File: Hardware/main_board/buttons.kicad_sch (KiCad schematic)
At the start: 0 parts

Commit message: sch: done buttons
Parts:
- added C77, C78: 10uF, symbol Device:C
- added C79: 100nF, symbol Device:C
- added D1, D2, D3, D4, D5, D6: TVS, symbol Device:D_TVS
- added D7, D8, D9: 1N4148, symbol Device:D
- added R20, R21, R22, R23, R24, R25, R35: 10K, symbol Device:R_US
- added R26, R27, R28, R29, R30, R31, R34: 330R, symbol Device:R_US
- added R32, R33: 100K, symbol Device:R_US
- added SW1: OK, symbol Switch:SW_Push
- added SW2: BACK, symbol Switch:SW_Push
- added SW3: RIGHT, symbol Switch:SW_Push
- added SW4: LEFT, symbol Switch:SW_Push
- added SW5: UP, symbol Switch:SW_Push
- added SW6: DOWN, symbol Switch:SW_Push
- added U12: NC7SZ32M5X, symbol 74xGxx:74AHC1G32
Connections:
- new net: C78.2, D8.1 (K), R33.1, U12.2
- new net: D3.2 (A2), R22.1, R28.2, SW3.1
- new net: D5.2 (A2), R24.1, R30.2, SW5.1
- new net: D1.2 (A2), R20.2, R26.2, SW1.1
- new net: C77.2, D7.1 (K), R32.1, U12.1
- new net: D6.2 (A2), R25.1, R31.2, SW6.1
- new net: D9.1 (K), U12.4
- new net: D9.2 (A), R34.2
- new net +3.3V: C79.1, R21.2, R22.2, R23.2, R24.2, R25.2, R35.2, SW1.2, U12.5 (VCC)
- new net BACK: D2.2 (A2), D7.2 (A), R21.1, R27.2, R32.2, SW2.1
- new net BUTTON_BACK: R27.1
- new net BUTTON_DOWN: R31.1
- new net BUTTON_LEFT: R28.1
- new net BUTTON_OK: R26.1
- new net BUTTON_RIGHT: R29.1
- new net BUTTON_UP: R30.1
- new net GND: C77.1, C78.1, C79.2, D1.1 (A1), D2.1 (A1), D3.1 (A1), D4.1 (A1), D5.1 (A1), D6.1 (A1), R20.1, SW2.2, SW3.2, SW4.2, SW5.2, SW6.2, U12.3 (GND)
- new net LEFT: D4.2 (A2), D8.2 (A), R23.1, R29.2, R33.2, SW4.1
- new net RESET: R34.1, R35.1
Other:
- note added: "Buttons"
- note added: "RESET"

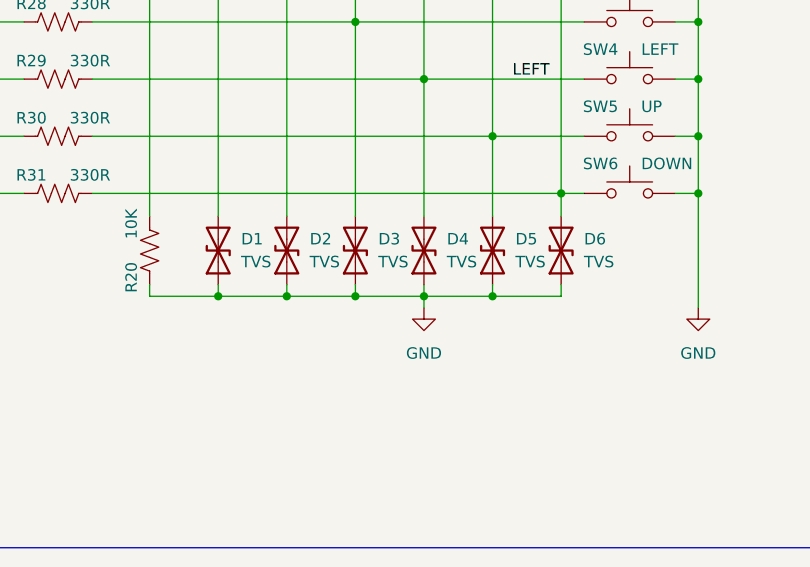
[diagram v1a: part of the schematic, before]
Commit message: sch: unify label style
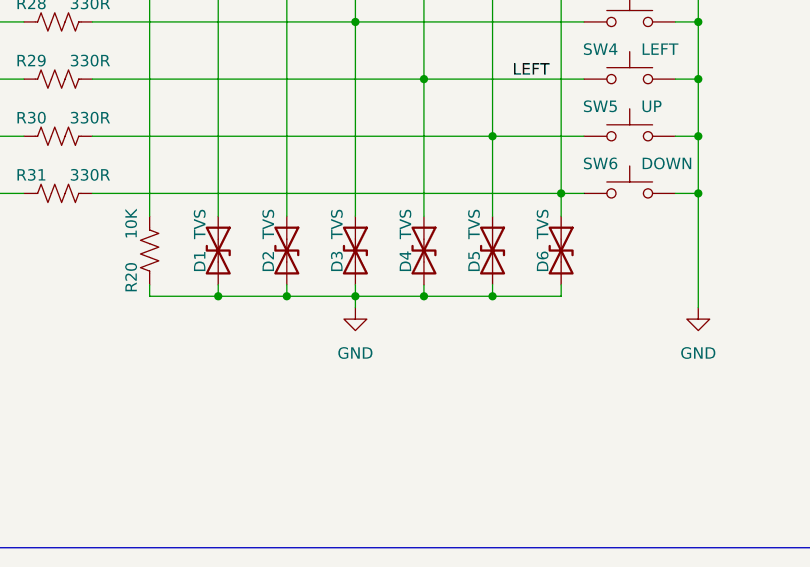
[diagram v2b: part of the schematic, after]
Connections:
- net BACK: now also D2.1 (A1); no longer D2.2 (A2)
- net GND: now also D1.2 (A2), D2.2 (A2), D3.2 (A2), D4.2 (A2), D5.2 (A2), D6.2 (A2); no longer D1.1 (A1), D2.1 (A1), D3.1 (A1), D4.1 (A1), D5.1 (A1), D6.1 (A1)
- net LEFT: now also D4.1 (A1); no longer D4.2 (A2)
- net at R22.1, R28.2, SW3.1: now also D3.1 (A1); no longer D3.2 (A2)
- net at R24.1, R30.2, SW5.1: now also D5.1 (A1); no longer D5.2 (A2)
- net at R20.2, R26.2, SW1.1: now also D1.1 (A1); no longer D1.2 (A2)
- net at R25.1, R31.2, SW6.1: now also D6.1 (A1); no longer D6.2 (A2)

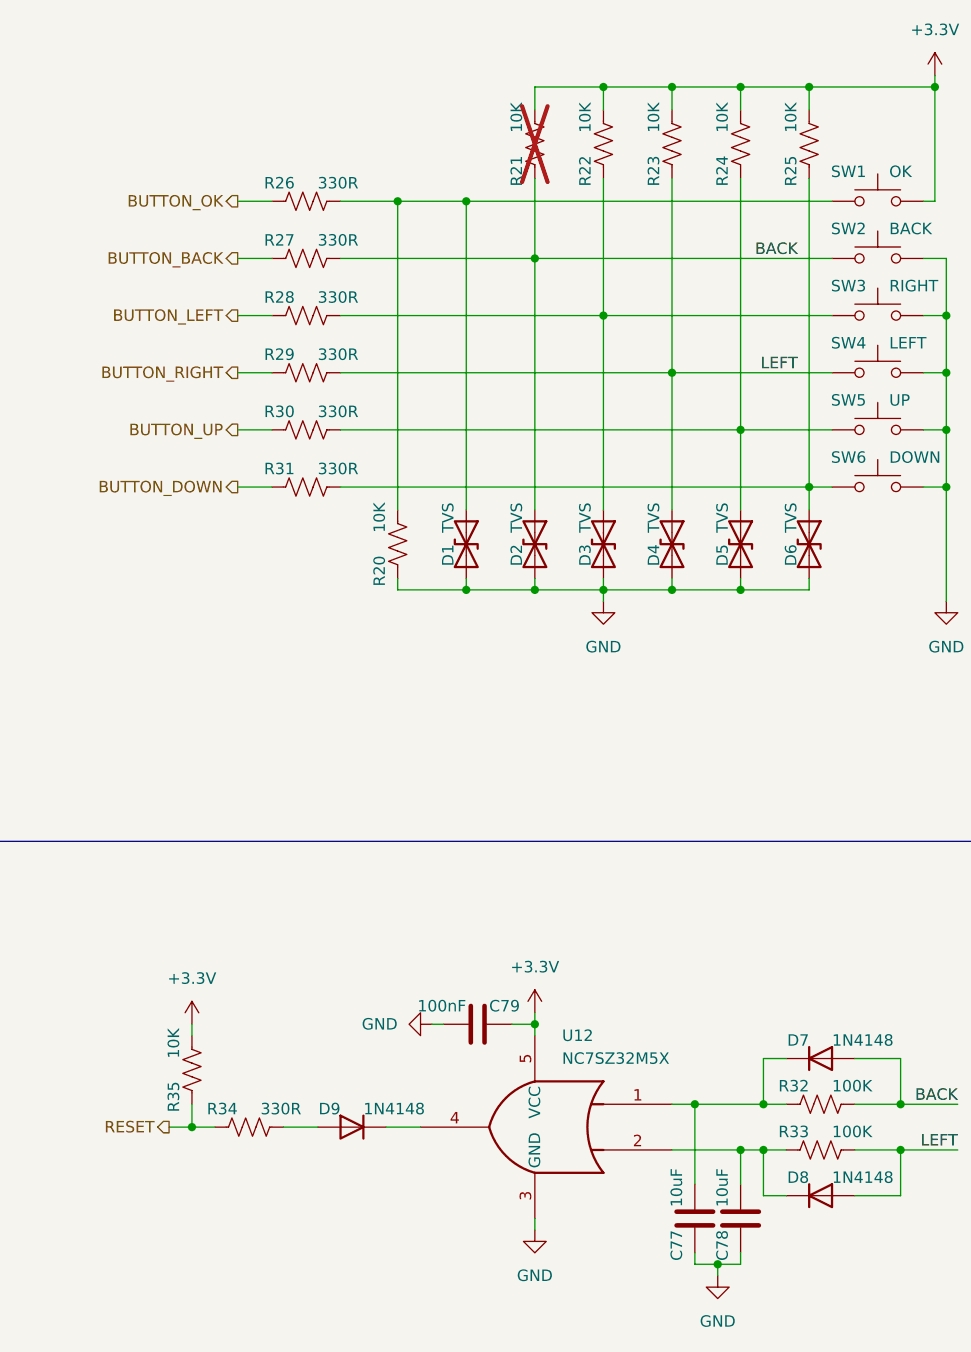
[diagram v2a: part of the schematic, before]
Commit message: sch: add some part of footprints
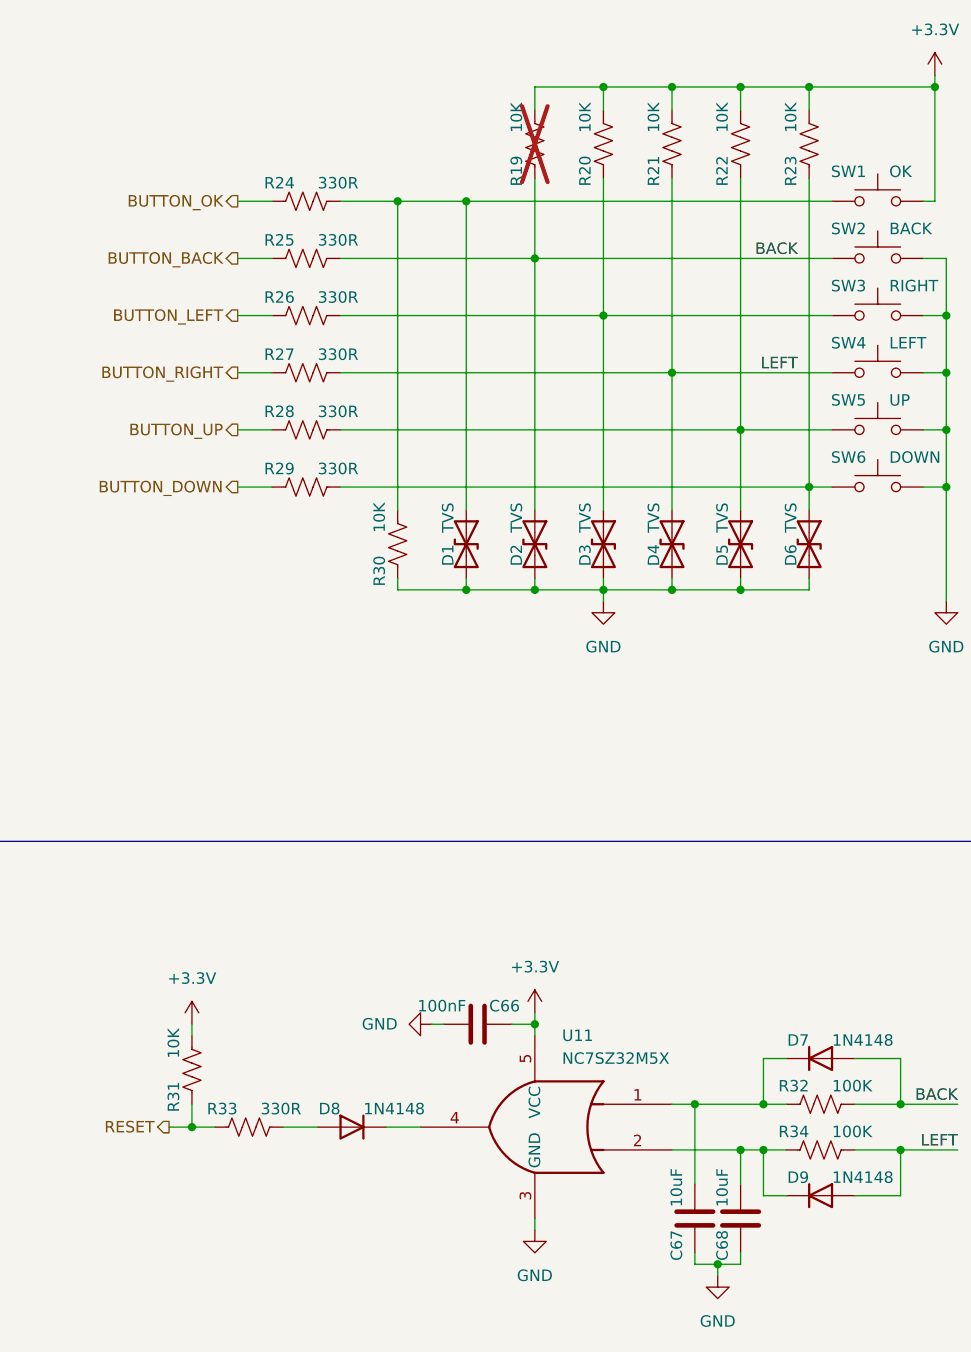
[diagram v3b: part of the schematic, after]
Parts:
- C66: renamed from C79; footprint (none) -> Capacitor_SMD:C_0402_1005Metric
- C67: renamed from C77; footprint (none) -> Capacitor_SMD:C_0603_1608Metric
- C68: renamed from C78; footprint (none) -> Capacitor_SMD:C_0603_1608Metric
- D1, D2, D3, D4, D5, D6: footprint (none) -> Diode_SMD:D_0201_0603Metric
- D7: footprint (none) -> Diode_SMD:D_SOD-523
- D8: renamed from D9; footprint (none) -> Diode_SMD:D_SOD-523
- D9: renamed from D8; footprint (none) -> Diode_SMD:D_SOD-523
- R19: renamed from R21; footprint (none) -> Resistor_SMD:R_0402_1005Metric
- R20: renamed from R22; footprint (none) -> Resistor_SMD:R_0402_1005Metric
- R21: renamed from R23; footprint (none) -> Resistor_SMD:R_0402_1005Metric
- R22: renamed from R24; footprint (none) -> Resistor_SMD:R_0402_1005Metric
- R23: renamed from R25; footprint (none) -> Resistor_SMD:R_0402_1005Metric
- R24: renamed from R26; footprint (none) -> Resistor_SMD:R_0402_1005Metric
- R25: renamed from R27; footprint (none) -> Resistor_SMD:R_0402_1005Metric
- R26: renamed from R28; footprint (none) -> Resistor_SMD:R_0402_1005Metric
- R27: renamed from R29; footprint (none) -> Resistor_SMD:R_0402_1005Metric
- R28: renamed from R30; footprint (none) -> Resistor_SMD:R_0402_1005Metric
- R29: renamed from R31; footprint (none) -> Resistor_SMD:R_0402_1005Metric
- R30: renamed from R20; footprint (none) -> Resistor_SMD:R_0402_1005Metric
- R31: renamed from R35; footprint (none) -> Resistor_SMD:R_0402_1005Metric
- R32: footprint (none) -> Resistor_SMD:R_0402_1005Metric
- R33: renamed from R34; footprint (none) -> Resistor_SMD:R_0402_1005Metric
- R34: renamed from R33; footprint (none) -> Resistor_SMD:R_0402_1005Metric
- renumbered U12 to U11

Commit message: sch: add more footprints
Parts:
- SW1: footprint (none) -> Button_Switch_SMD:SW_Push_SPST_NO_Alps_SKRK
- SW2, SW3, SW4, SW5, SW6: footprint (none) -> Library:SW_Push_SPST_NO_Alps_ SKRM
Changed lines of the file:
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@@
 			)
 		)
-		(property "Footprint" ""
+		(property "Footprint" "Library:SW_Push_SPST_NO_Alps_ SKRM"
 			(at 153.67 69.85 0)
 			(effects
@@
 			)
 		)
-		(property "Footprint" ""
+		(property "Footprint" "Button_Switch_SMD:SW_Push_SPST_NO_Alps_SKRK"
 			(at 153.67 50.8 0)
 			(effects
@@
 			)
 		)
-		(property "Footprint" ""
+		(property "Footprint" "Library:SW_Push_SPST_NO_Alps_ SKRM"
 			(at 153.67 82.55 0)
 			(effects
@@
 			)
 		)
-		(property "Footprint" ""
+		(property "Footprint" "Library:SW_Push_SPST_NO_Alps_ SKRM"
 			(at 153.67 63.5 0)
 			(effects
@@
 			)
 		)
-		(property "Footprint" ""
+		(property "Footprint" "Library:SW_Push_SPST_NO_Alps_ SKRM"
 			(at 153.67 57.15 0)
 			(effects
@@
 			)
 		)
-		(property "Footprint" ""
+		(property "Footprint" "Library:SW_Push_SPST_NO_Alps_ SKRM"
 			(at 153.67 76.2 0)
 			(effects

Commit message: layout: change some of the footprint and start to layout
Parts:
- U11: footprint (none) -> Package_TO_SOT_SMD:SOT-23-5
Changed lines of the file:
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@@
 			)
 		)
-		(property "Footprint" ""
+		(property "Footprint" "Package_TO_SOT_SMD:SOT-23-5"
 			(at 115.57 158.75 0)
 			(effects

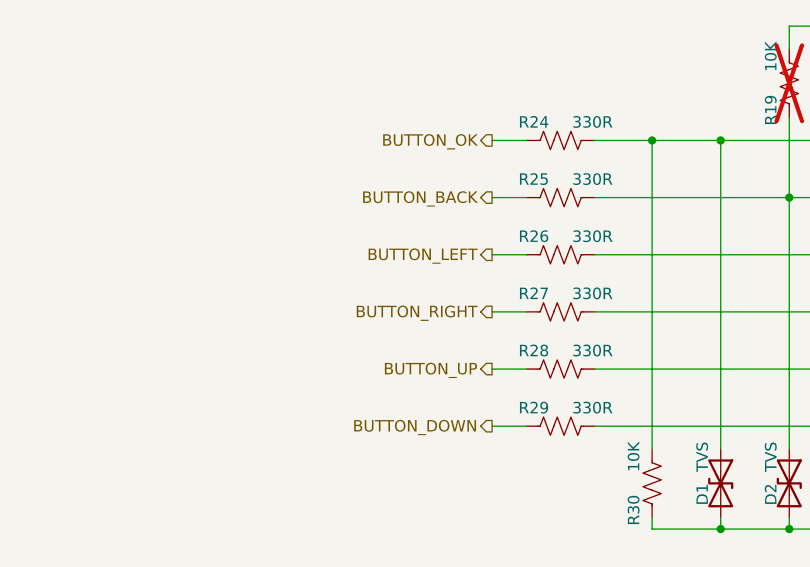
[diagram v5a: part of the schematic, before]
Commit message: sch: fix swapd buttons
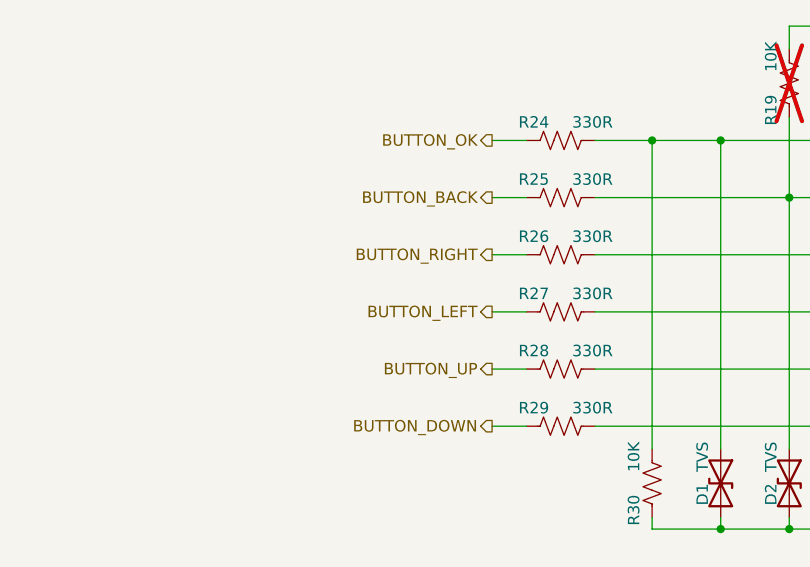
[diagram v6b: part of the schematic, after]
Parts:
- SW1: footprint Button_Switch_SMD:SW_Push_SPST_NO_Alps_SKRK -> Library:SW_Push_SPST_NO_Alps_ SKRM
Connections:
- net BUTTON_LEFT: now also R27.1; no longer R26.1
- net BUTTON_RIGHT: now also R26.1; no longer R27.1
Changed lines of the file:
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@@
 	(hierarchical_label "BUTTON_LEFT"
 		(shape output)
-		(at 82.55 68.58 180)
+		(at 82.55 74.93 180)
 		(fields_autoplaced yes)
 		(effects
@@
 	(hierarchical_label "BUTTON_RIGHT"
 		(shape output)
-		(at 82.55 74.93 180)
+		(at 82.55 68.58 180)
 		(fields_autoplaced yes)
 		(effects
@@
 			)
 		)
-		(property "Footprint" "Button_Switch_SMD:SW_Push_SPST_NO_Alps_SKRK"
+		(property "Footprint" "Library:SW_Push_SPST_NO_Alps_ SKRM"
 			(at 153.67 50.8 0)
 			(effects

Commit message: sch: change some footprints
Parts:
- C67, C68: footprint Capacitor_SMD:C_0603_1608Metric -> Capacitor_SMD:C_0402_1005Metric
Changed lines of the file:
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@@
 			)
 		)
-		(property "Footprint" "Capacitor_SMD:C_0603_1608Metric"
+		(property "Footprint" "Capacitor_SMD:C_0402_1005Metric"
 			(at 137.4648 165.1 0)
 			(effects
@@
 			)
 		)
-		(property "Footprint" "Capacitor_SMD:C_0603_1608Metric"
+		(property "Footprint" "Capacitor_SMD:C_0402_1005Metric"
 			(at 132.3848 165.1 0)
 			(effects
